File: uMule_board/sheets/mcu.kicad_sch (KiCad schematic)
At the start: 29 parts, among them SW2 DBG_BUTT, SW3 RST, U15 STM32F103RCTx, U23 FM24C64B, Y1 8MHz

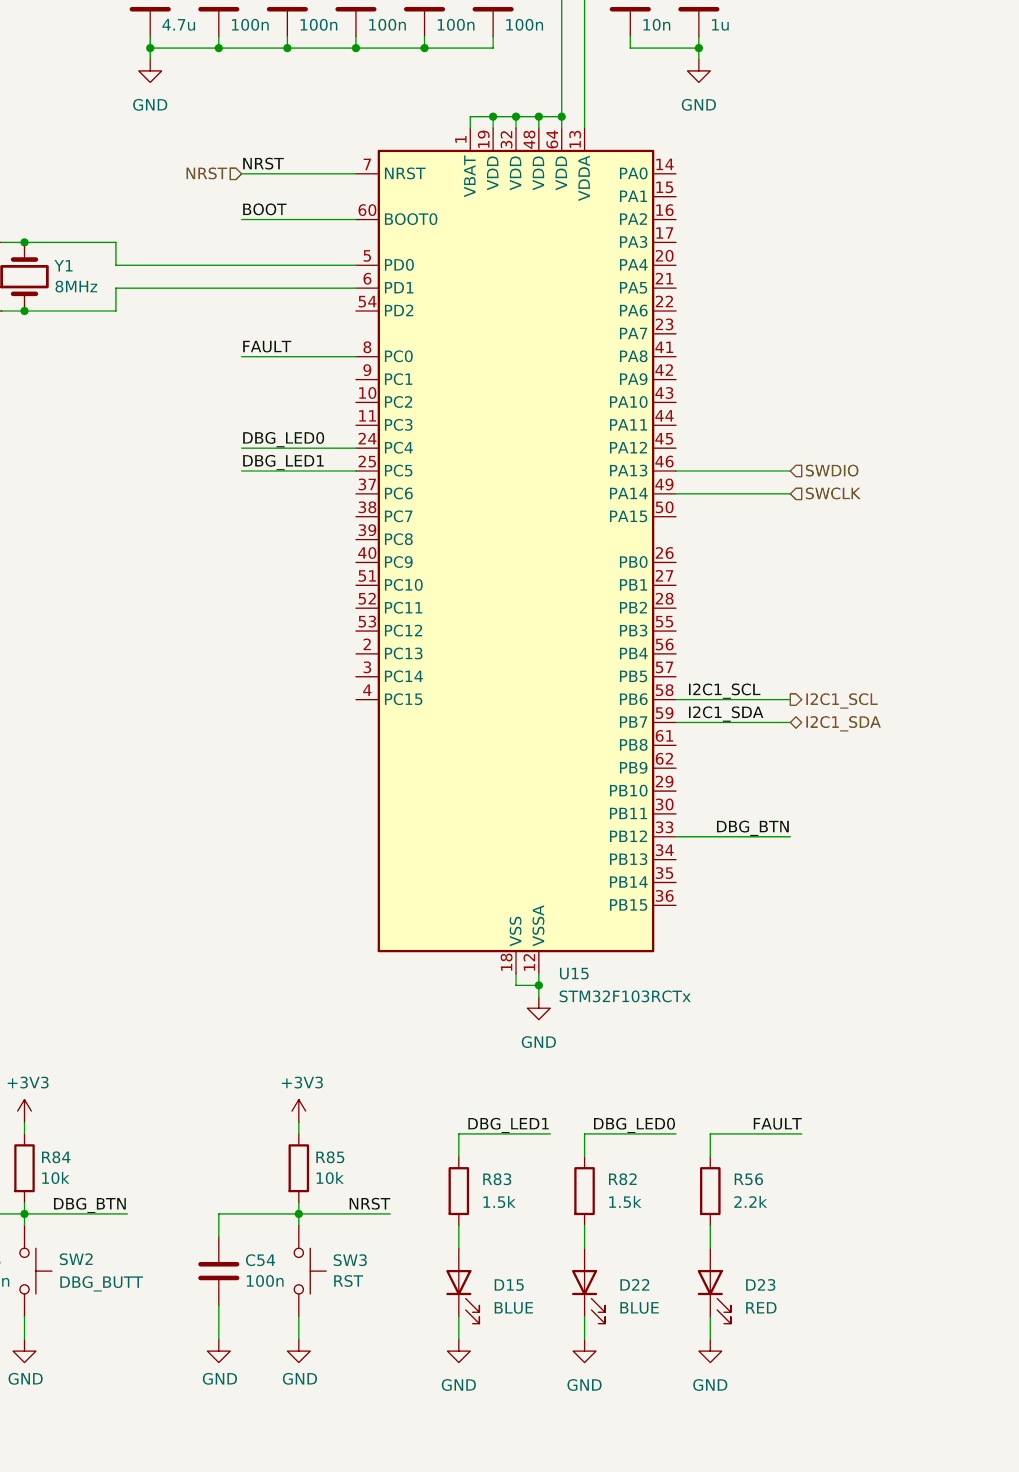
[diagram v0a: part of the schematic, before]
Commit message: addd buses and simple connections
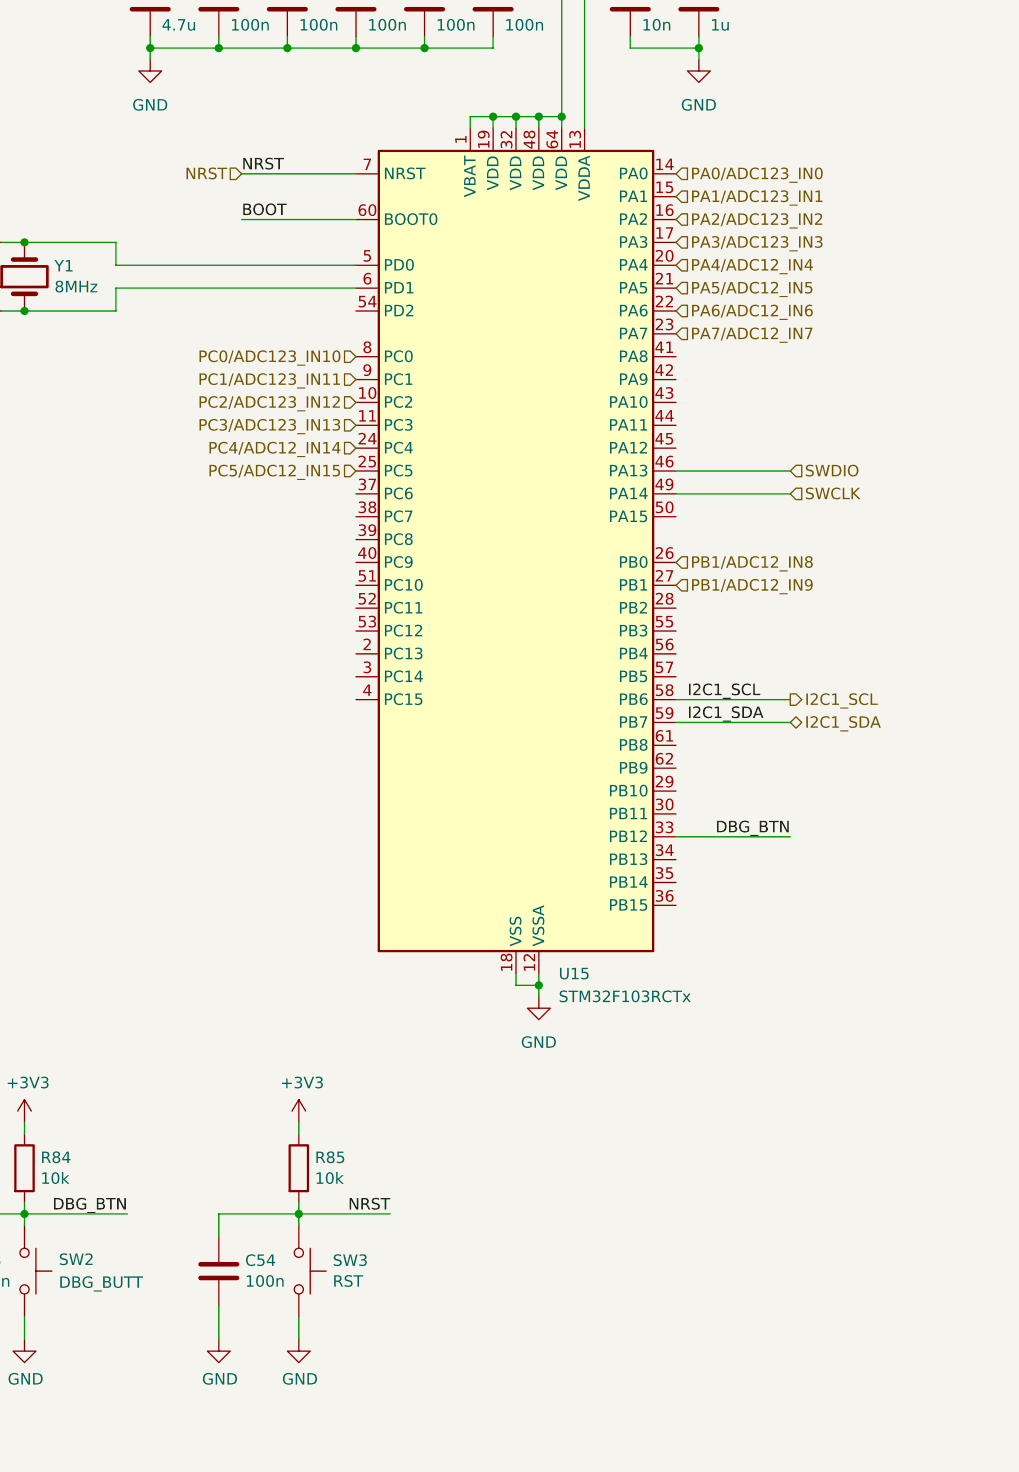
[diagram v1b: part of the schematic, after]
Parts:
- removed D15, D22: BLUE, LED_SMD:LED_0603_1608Metric, symbol Device:LED
- removed D23: RED, LED_SMD:LED_0603_1608Metric, symbol Device:LED
- removed R56: 2.2k, Resistor_SMD:R_0603_1608Metric, symbol Device:R
- removed R82, R83: 1.5k, Resistor_SMD:R_0603_1608Metric, symbol Device:R
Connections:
- net PC2/ADC123_IN12: now reaches U15.10 (PC2)
- net PC3/ADC123_IN13: now reaches U15.11 (PC3)
- net PA0/ADC123_IN0: now reaches U15.14 (PA0)
- net PA1/ADC123_IN1: now reaches U15.15 (PA1)
- net PA2/ADC123_IN2: now reaches U15.16 (PA2)
- net PA3/ADC123_IN3: now reaches U15.17 (PA3)
- net PA4/ADC12_IN4: now reaches U15.20 (PA4)
- net PA5/ADC12_IN5: now reaches U15.21 (PA5)
- net PA6/ADC12_IN6: now reaches U15.22 (PA6)
- net PA7/ADC12_IN7: now reaches U15.23 (PA7)
- net PB1/ADC12_IN8: now reaches U15.26 (PB0)
- net PB1/ADC12_IN9: now reaches U15.27 (PB1)
- net PC1/ADC123_IN11: now reaches U15.9 (PC1)
- net DBG_LED0 renamed PC4/ADC12_IN14
- net DBG_LED1 renamed PC5/ADC12_IN15
- net FAULT renamed PC0/ADC123_IN10

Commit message: Some calculations were made. Photodiode, amplifier and main procesor are chosen
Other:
- note added: "Powinno być *RET"
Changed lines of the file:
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@@
+		)
+	)
+	(text "Powinno być *RET"
+		(exclude_from_sim no)
+		(at 157.988 147.32 0)
+		(effects
+			(font
+				(size 1.27 1.27)
+			)
 		)
 	)

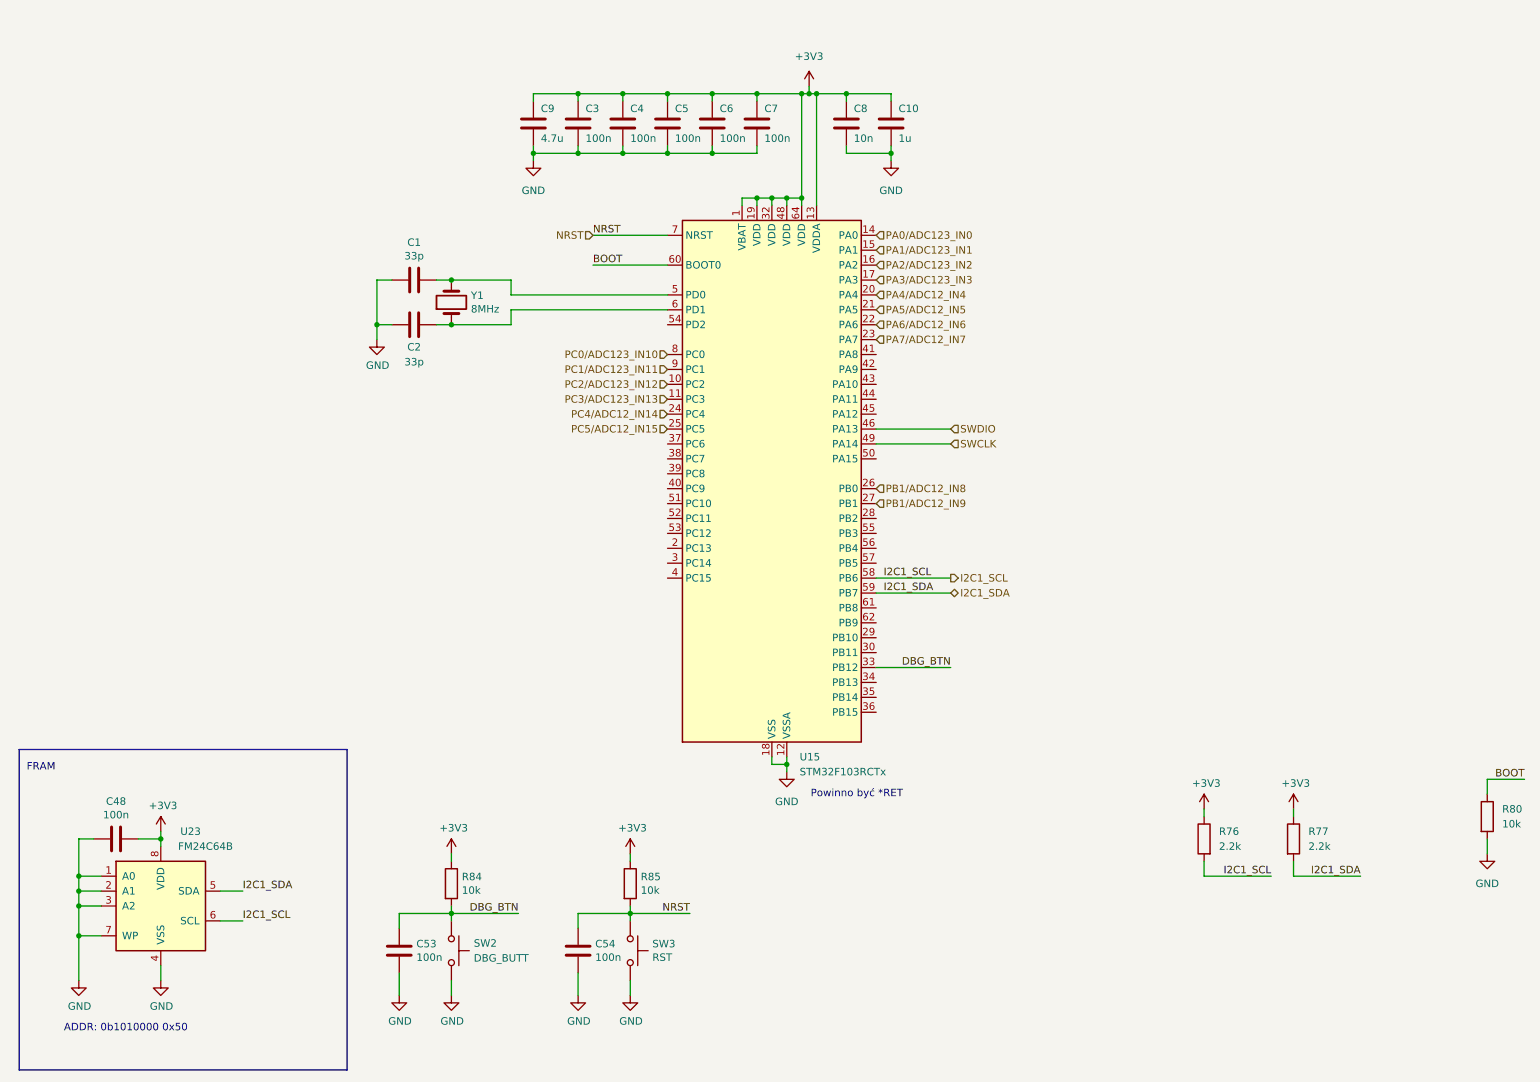
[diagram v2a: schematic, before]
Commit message: all main componenst added. Prepared to change MCU. SCH almost ready
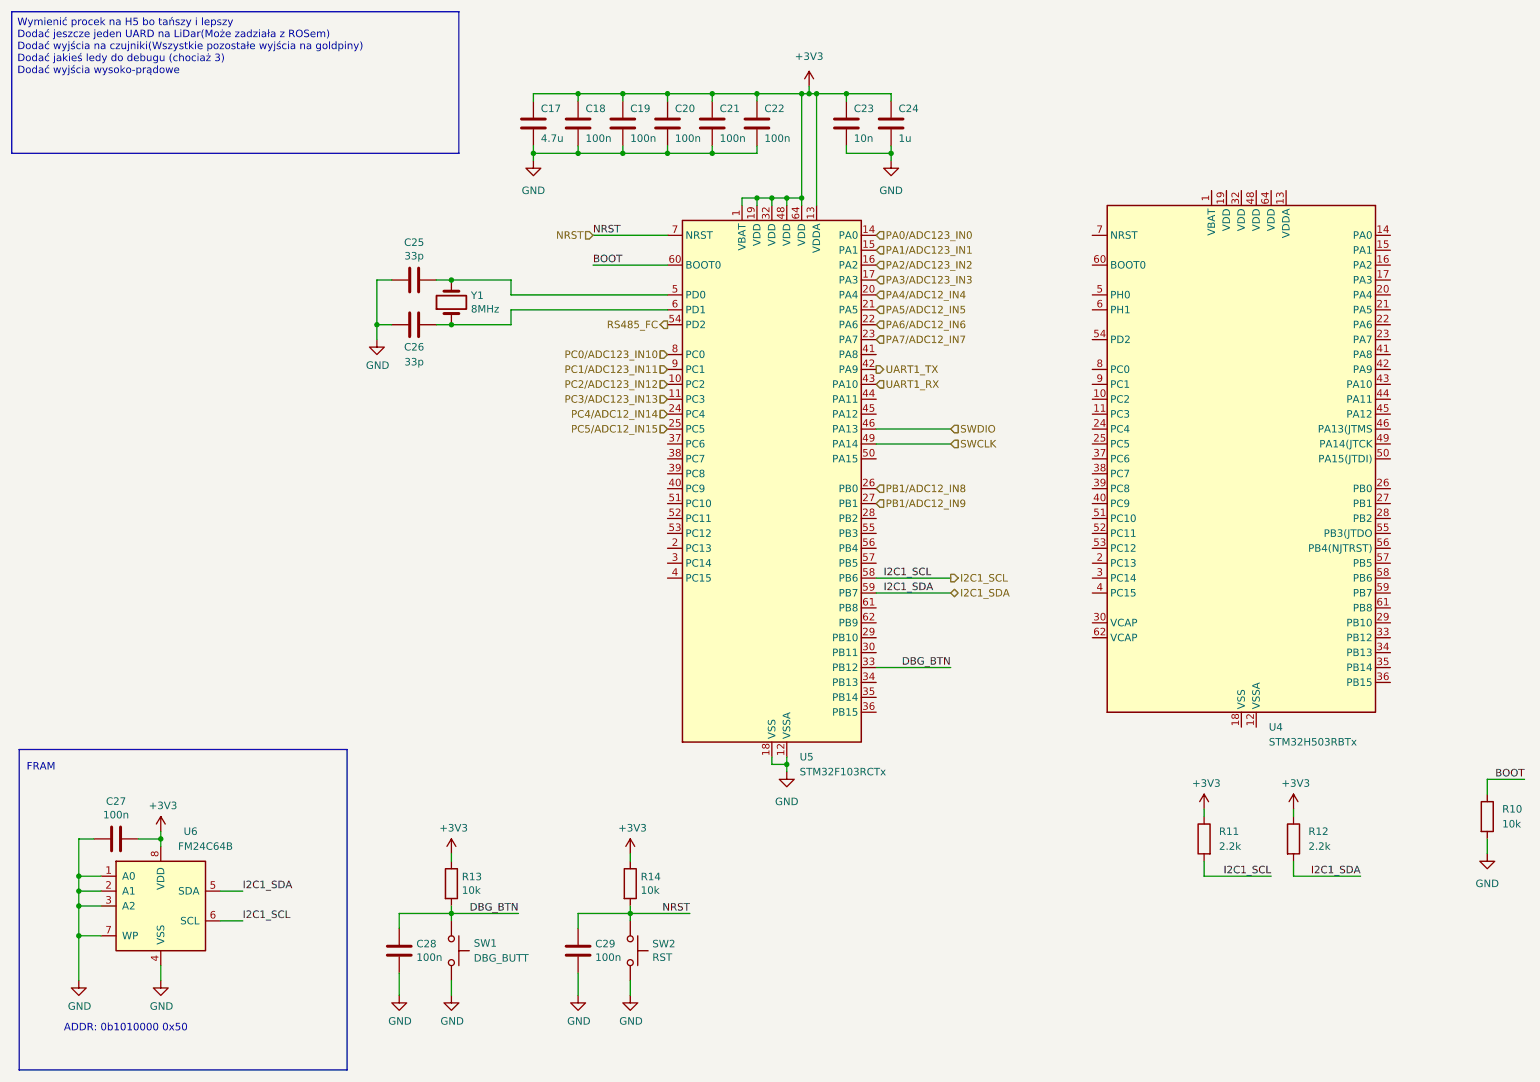
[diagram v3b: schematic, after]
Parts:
- added U4: STM32H503RBTx, Package_QFP:LQFP-64_10x10mm_P0.5mm, symbol MCU_ST_STM32H5:STM32H503RBTx
- renumbered C9 to C17, C3 to C18, C4 to C19, C5 to C20, C6 to C21, C7 to C22, C8 to C23, C10 to C24, C1 to C25, C2 to C26, C48 to C27, C53 to C28, C54 to C29, R80 to R10, R76 to R11, R77 to R12, R84 to R13, R85 to R14, SW2 to SW1, SW3 to SW2, U15 to U5, U23 to U6
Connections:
- net UART1_TX: now reaches U5.42 (PA9)
- net UART1_RX: now reaches U5.43 (PA10)
- net RS485_FC: now reaches U5.54 (PD2)
- new net: U4.18 (VSS), U4.31 (VSS), U4.47 (VSS), U4.63 (VSS)
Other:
- note removed: "Powinno być *RET"

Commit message: Finished schematics. Now ready for PCB
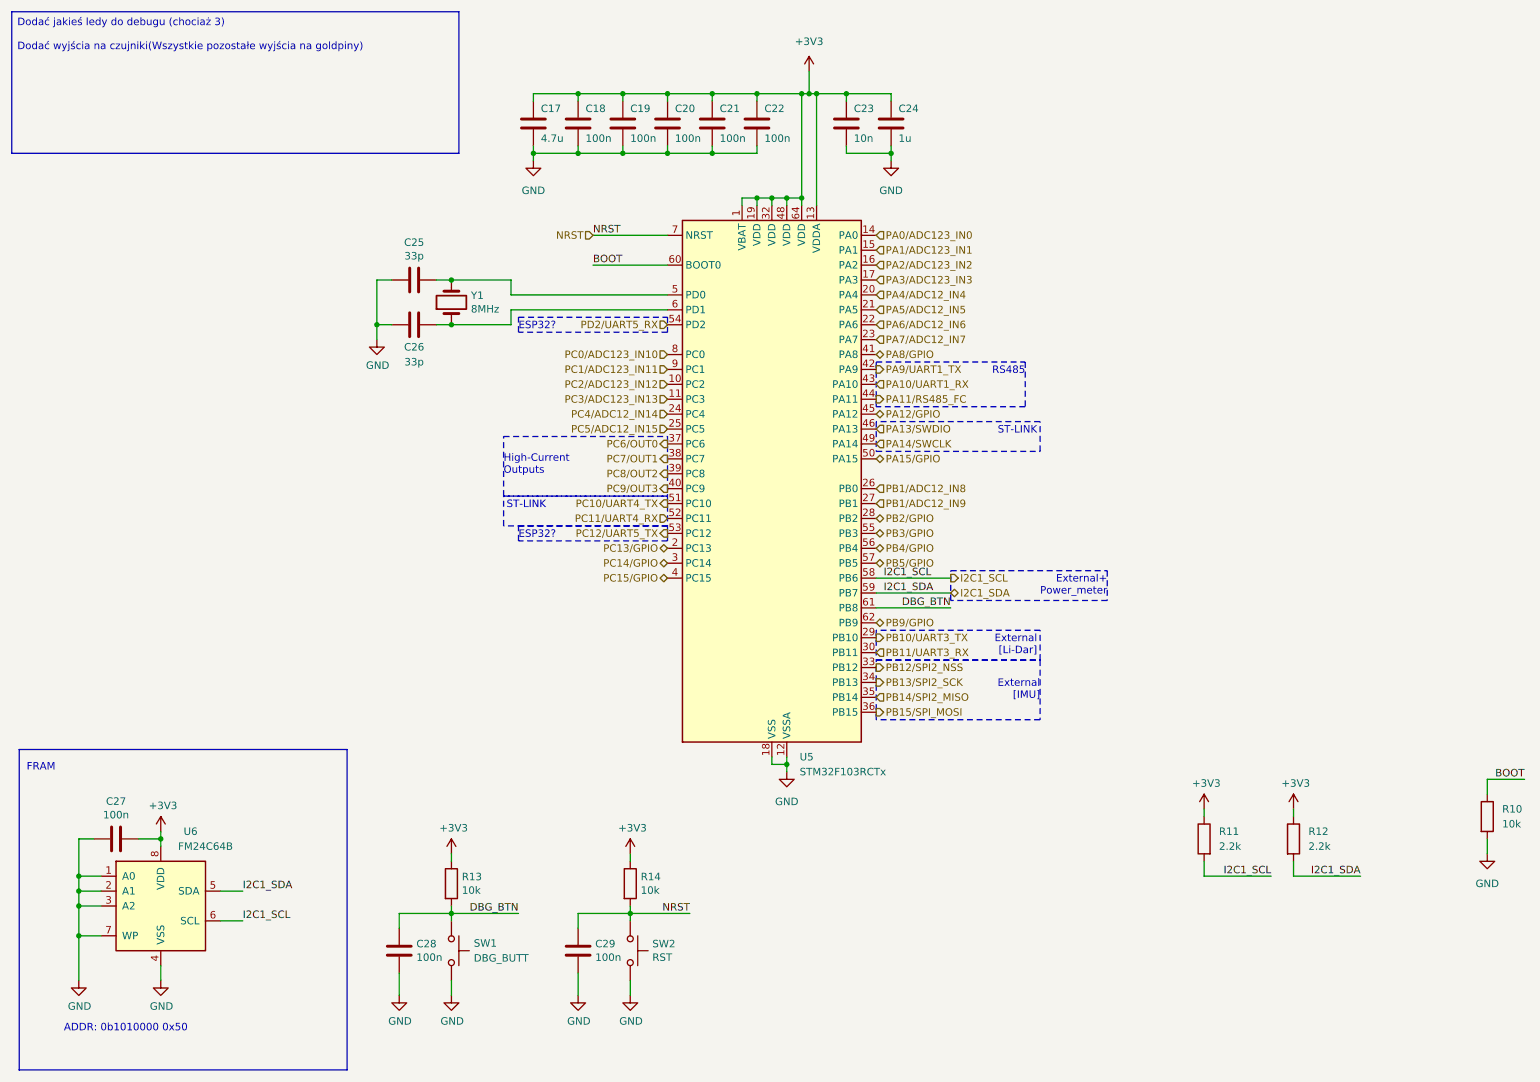
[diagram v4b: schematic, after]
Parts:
- removed U4: STM32H503RBTx, Package_QFP:LQFP-64_10x10mm_P0.5mm, symbol MCU_ST_STM32H5:STM32H503RBTx
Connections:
- net DBG_BTN: now also U5.61 (PB8); no longer U5.33 (PB12)
- net PC13/GPIO: now reaches U5.2 (PC13)
- net PB2/GPIO: now reaches U5.28 (PB2)
- net PB10/UART3_TX: now reaches U5.29 (PB10)
- net PC14/GPIO: now reaches U5.3 (PC14)
- net PB11/UART3_RX: now reaches U5.30 (PB11)
- net PB13/SPI2_SCK: now reaches U5.34 (PB13)
- net PB14/SPI2_MISO: now reaches U5.35 (PB14)
- net PB15/SPI_MOSI: now reaches U5.36 (PB15)
- net PC6/OUT0: now reaches U5.37 (PC6)
- net PC7/OUT1: now reaches U5.38 (PC7)
- net PC8/OUT2: now reaches U5.39 (PC8)
- net PC15/GPIO: now reaches U5.4 (PC15)
- net PC9/OUT3: now reaches U5.40 (PC9)
- net PA8/GPIO: now reaches U5.41 (PA8)
- net PA11/RS485_FC: now reaches U5.44 (PA11)
- net PA12/GPIO: now reaches U5.45 (PA12)
- net PA15/GPIO: now reaches U5.50 (PA15)
- net PC10/UART4_TX: now reaches U5.51 (PC10)
- net PC11/UART4_RX: now reaches U5.52 (PC11)
- net PC12/UART5_TX: now reaches U5.53 (PC12)
- net PB3/GPIO: now reaches U5.55 (PB3)
- net PB4/GPIO: now reaches U5.56 (PB4)
- net PB5/GPIO: now reaches U5.57 (PB5)
- net PB9/GPIO: now reaches U5.62 (PB9)
- net RS485_FC renamed PD2/UART5_RX
- net SWCLK renamed PA14/SWCLK
- net SWDIO renamed PA13/SWDIO
- net UART1_RX renamed PA10/UART1_RX
- net UART1_TX renamed PA9/UART1_TX
- new net PB12/SPI2_NSS: U5.33 (PB12)
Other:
- note added: "ESP32?"
- note added: "External [IMU]"
- note added: "External [Li-Dar]"
- note added: "External+ Power_meter"
- note added: "High-Current Outputs"
- note added: "RS485"
- note added: "ST-LINK"
